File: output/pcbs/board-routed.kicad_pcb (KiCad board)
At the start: 2 copper layers, 141.8 x 108.1 mm, 40 parts

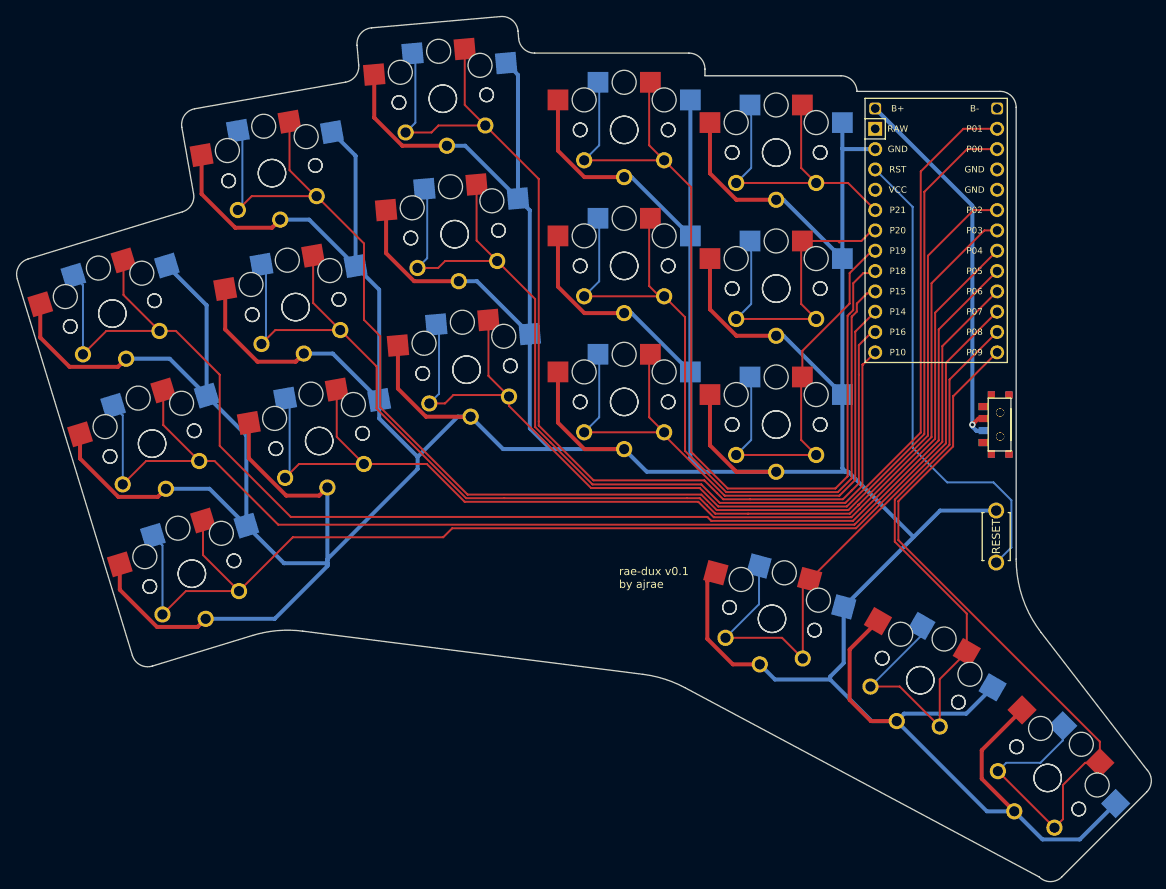
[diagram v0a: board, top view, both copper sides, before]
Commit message: Routed new design with battery connectors.
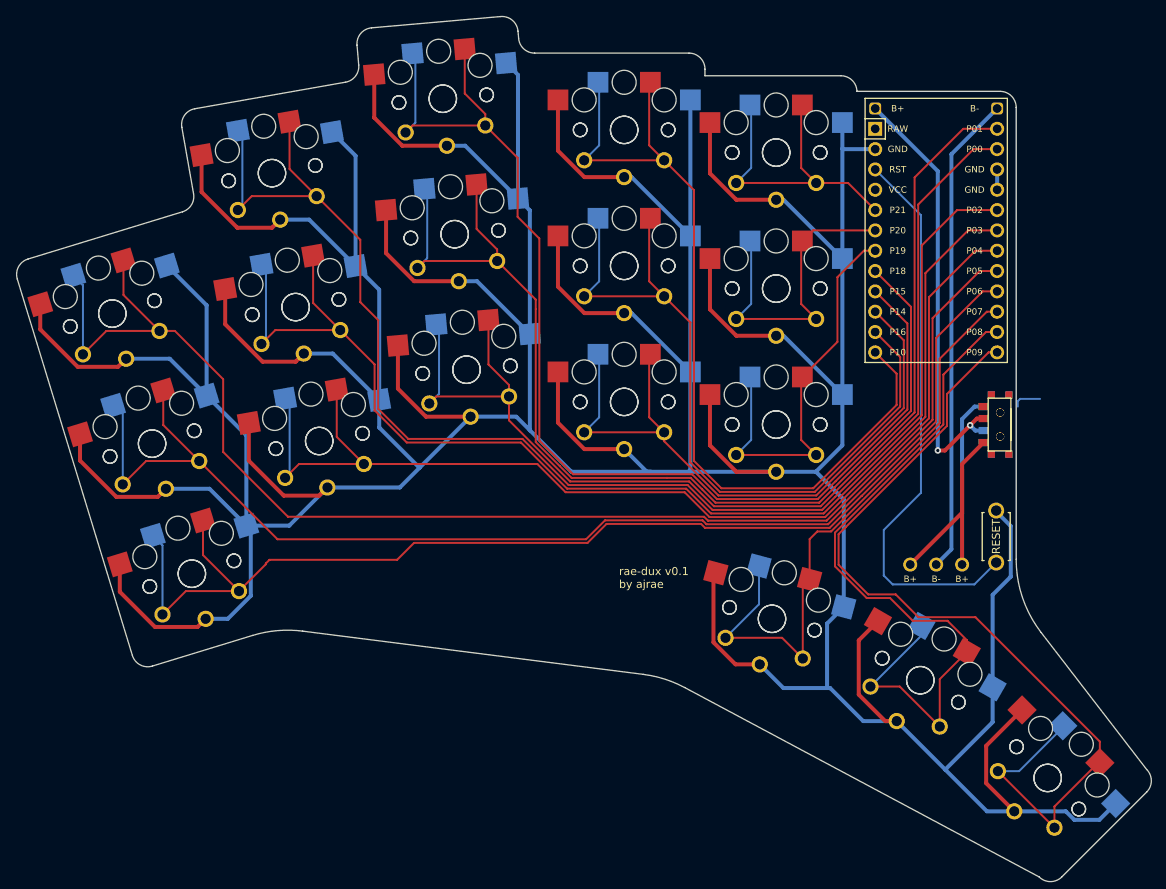
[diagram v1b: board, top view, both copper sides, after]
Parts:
- added PAD1: , lib:bat, F.Cu at (106.1, -0.40)
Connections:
- MCU1 pad 25: Bminus -> Bplus
- S15 pad 1: P10 -> P18
- S16 pad 1: P10 -> P18
- S17 pad 1: P16 -> P15
- S18 pad 1: P16 -> P15
- S21 pad 1: P15 -> P16
- S22 pad 1: P15 -> P16
- S23 pad 1: P18 -> P10
- S24 pad 1: P18 -> P10
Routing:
- net Bminus: track 0.00 -> 60.2 mm
- net Braw: track 0.00 -> 52.4 mm
- net P15: track 98.8 -> 143.7 mm
- net P16: track 135.6 -> 96.1 mm
- net GND: track 869.9 -> 854.7 mm
- net P18: track 118.1 -> 130.3 mm
- net P8: track 80.7 -> 92.0 mm
- net P9: track 99.9 -> 111.0 mm
- net RST: track 60.4 -> 70.7 mm
- net P10: track 117.3 -> 109.0 mm
- net Bplus: track 48.2 -> 55.3 mm, vias 1 -> 2
- net (no net): track 0.00 -> 3.57 mm
- net P19: track 49.4 -> 51.6 mm
- net P7: track 74.9 -> 76.6 mm
- net P14: track 81.4 -> 83.1 mm
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
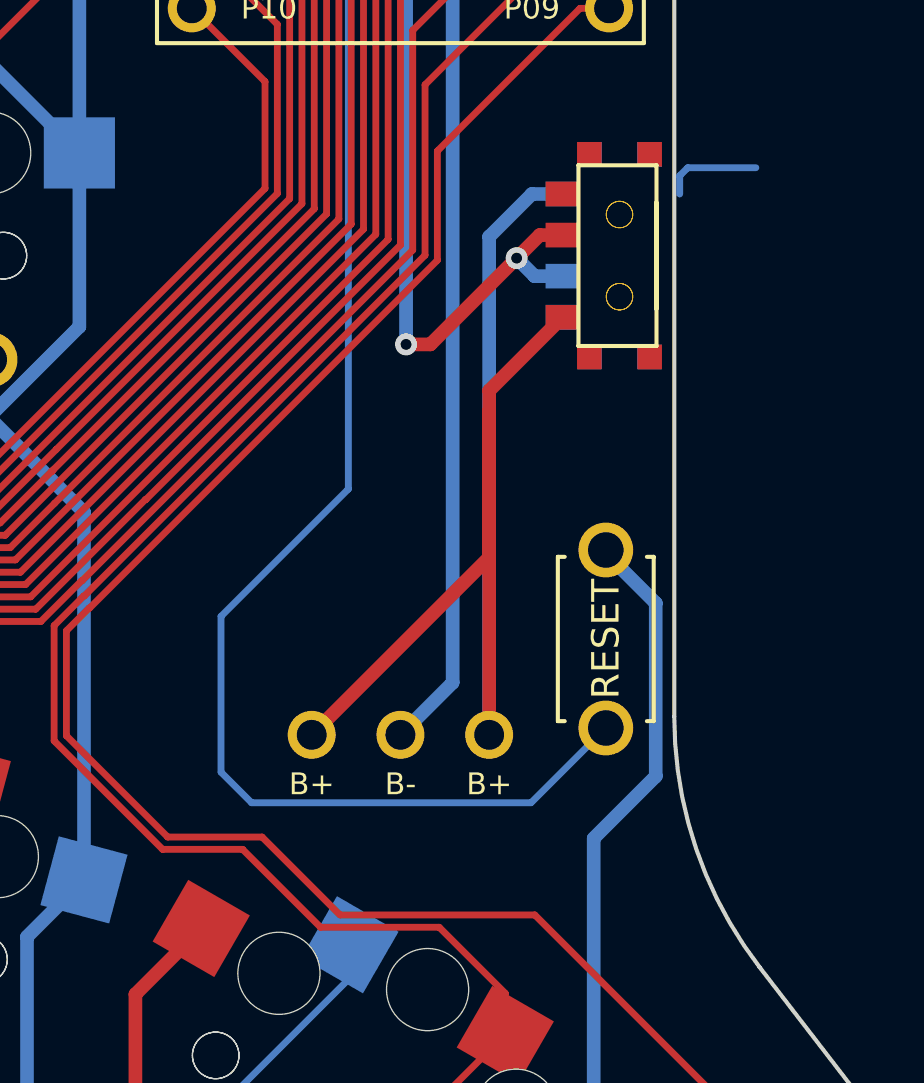
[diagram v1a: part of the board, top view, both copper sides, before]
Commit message: Cleaning up board a little.
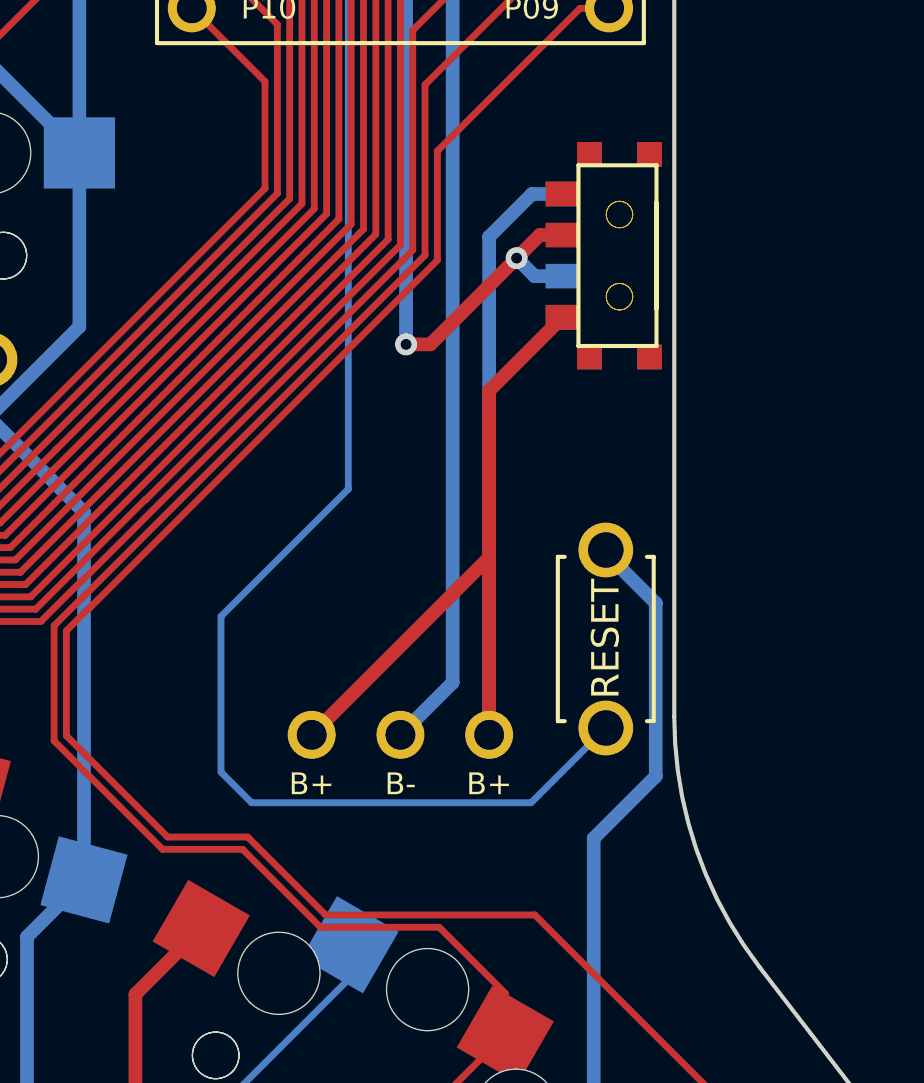
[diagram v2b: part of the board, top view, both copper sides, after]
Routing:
- net (no net): track 3.57 -> 0.00 mm
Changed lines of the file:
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@@
     (effects (font (size 1 1) (thickness 0.15)) (justify left))
   )
-  (segment (start 116.5606 -21.1074) (end 116.26738 -20.81418) (width 0.25) (layer "B.Cu") (net 0))
-  (segment (start 116.26738 -20.81418) (end 116.26738 -20.147422) (width 0.25) (layer "B.Cu") (net 0))
-  (segment (start 119.0498 -21.1074) (end 116.5606 -21.1074) (width 0.25) (layer "B.Cu") (net 0))
   (segment (start 12.282887 2.914919) (end 9.35917 5.838636) (width 0.25) (layer "F.Cu") (net 1))
   (segment (start 96.756494 -8.9916) (end 96.774 -8.9916) (width 0.25) (layer "F.Cu") (net 1))
@@
   (segment (start 104.224185 7.268496) (end 104.224185 8.48085) (width 0.25) (layer "B.Cu") (net 18))
   (segment (start 126.31562 24.382106) (end 126.527076 24.382106) (width 0.25) (layer "F.Cu") (net 19))
-  (segment (start 97.569798 3.33508) (end 101.0158 3.33508) (width 0.25) (layer "F.Cu") (net 19))
+  (segment (start 93.87072 -4.198674) (end 93.87072 -0.363998) (width 0.25) (layer "F.Cu") (net 19))
+  (segment (start 120.852544 29.845182) (end 126.31562 24.382106) (width 0.25) (layer "F.Cu") (net 19))
+  (segment (start 93.87072 -0.363998) (end 97.569798 3.33508) (width 0.25) (layer "F.Cu") (net 19))
+  (segment (start 120.852544 32.496157) (end 113.781476 25.425089) (width 0.25) (layer "F.Cu") (net 19))
+  (segment (start 126.527076 21.731133) (end 126.527076 24.382106) (width 0.25) (layer "F.Cu") (net 19))
+  (segment (start 110.975823 6.17988) (end 126.527076 21.731133) (width 0.25) (layer "F.Cu") (net 19))
+  (segment (start 120.852544 32.496157) (end 120.852544 29.845182) (width 0.25) (layer "F.Cu") (net 19))
+  (segment (start 107.4166 -17.727048) (end 94.713729 -5.024177) (width 0.25) (layer "F.Cu") (net 19))
+  (segment (start 97.569798 3.33508) (end 100.490798 3.33508) (width 0.25) (layer "F.Cu") (net 19))
+  (segment (start 103.335598 6.17988) (end 110.975823 6.17988) (width 0.25) (layer "F.Cu") (net 19))
   (segment (start 112.627023 -26.927423) (end 107.4166 -21.717) (width 0.25) (layer "F.Cu") (net 19))
-  (segment (start 120.852544 29.845182) (end 126.31562 24.382106) (width 0.25) (layer "F.Cu") (net 19))
-  (segment (start 120.852544 32.496157) (end 113.781476 25.425089) (width 0.25) (layer "F.Cu") (net 19))
+  (segment (start 94.713729 -5.024177) (end 94.696223 -5.024177) (width 0.25) (layer "F.Cu") (net 19))
+  (segment (start 107.4166 -21.717) (end 107.4166 -17.727048) (width 0.25) (layer "F.Cu") (net 19))
+  (segment (start 100.490798 3.33508) (end 103.335598 6.17988) (width 0.25) (layer "F.Cu") (net 19))
   (segment (start 94.696223 -5.024177) (end 93.87072 -4.198674) (width 0.25) (layer "F.Cu") (net 19))
-  (segment (start 107.4166 -17.727048) (end 94.713729 -5.024177) (width 0.25) (layer "F.Cu") (net 19))
-  (segment (start 107.4166 -21.717) (end 107.4166 -17.727048) (width 0.25) (layer "F.Cu") (net 19))
-  (segment (start 120.852544 32.496157) (end 120.852544 29.845182) (width 0.25) (layer "F.Cu") (net 19))
-  (segment (start 126.527076 21.731133) (end 126.527076 24.382106) (width 0.25) (layer "F.Cu") (net 19))
-  (segment (start 94.713729 -5.024177) (end 94.696223 -5.024177) (width 0.25) (layer "F.Cu") (net 19))
   (segment (start 113.68786 -26.927423) (end 112.627023 -26.927423) (width 0.25) (layer "F.Cu") (net 19))
-  (segment (start 101.0158 3.33508) (end 103.8606 6.17988) (width 0.25) (layer "F.Cu") (net 19))
-  (segment (start 93.87072 -0.363998) (end 97.569798 3.33508) (width 0.25) (layer "F.Cu") (net 19))
-  (segment (start 103.8606 6.17988) (end 110.975823 6.17988) (width 0.25) (layer "F.Cu") (net 19))
-  (segment (start 93.87072 -4.198674) (end 93.87072 -0.363998) (width 0.25) (layer "F.Cu") (net 19))
-  (segment (start 110.975823 6.17988) (end 126.527076 21.731133) (width 0.25) (layer "F.Cu") (net 19))
   (segment (start 116.432451 25.425089) (end 113.781476 25.425089) (width 0.25) (layer "B.Cu") (net 19))
   (segment (start 121.895527 19.750557) (end 121.895527 19.962013) (width 0.25) (layer "B.Cu") (net 19))

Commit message: Cleaning up the board even more.
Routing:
- net GND: track 854.7 -> 867.7 mm
- net P5: track 157.7 -> 158.3 mm
- net P4: track 174.5 -> 175.0 mm
